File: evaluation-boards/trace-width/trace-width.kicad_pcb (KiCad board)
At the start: 4 copper layers, 80 x 90 mm, 12 parts, among them J1 CONN_COAXIAL, J10 CONN_COAXIAL, J11 CONN_COAXIAL, J12 CONN_COAXIAL, J2 CONN_COAXIAL, J3 CONN_COAXIAL, J4 CONN_COAXIAL, J5 CONN_COAXIAL, J6 CONN_COAXIAL, J7 CONN_COAXIAL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

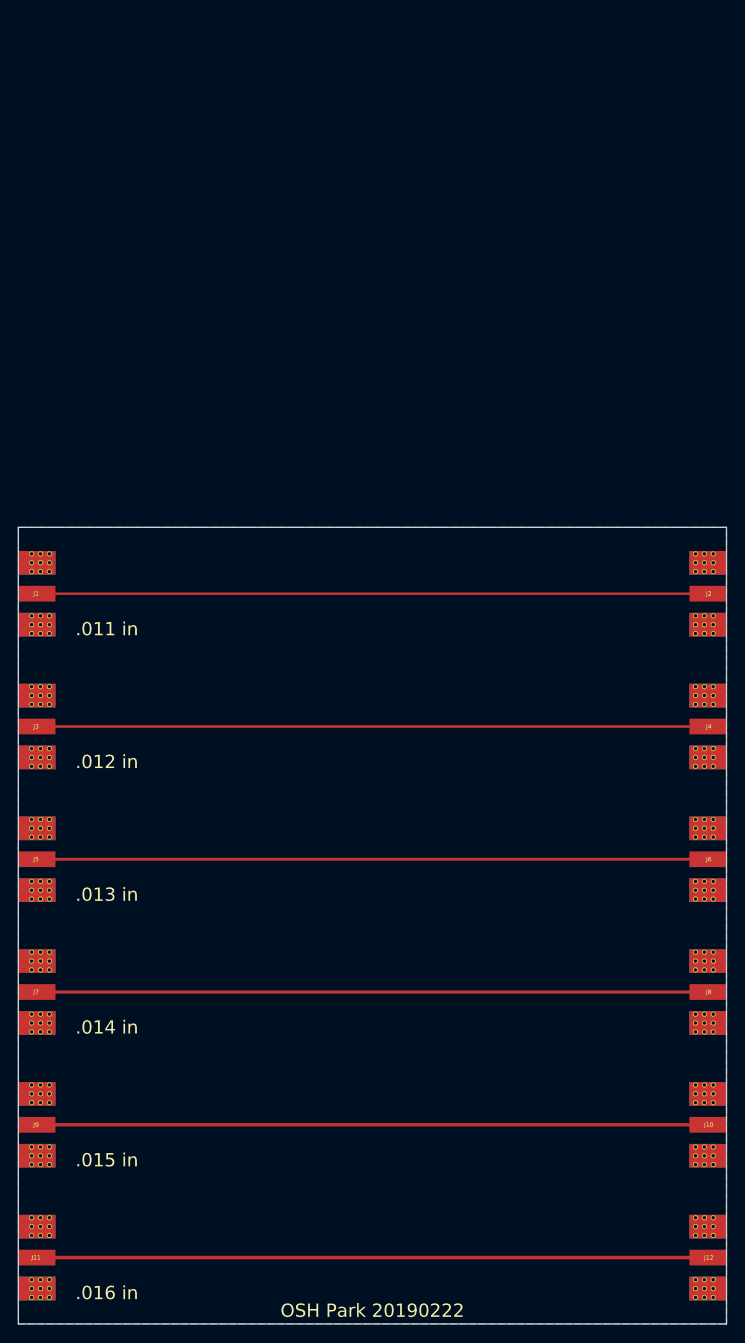
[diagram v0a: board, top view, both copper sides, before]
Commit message: update trace width test board
- widen traces
- use metric widths
- revert to CONSMA003.062 footprint
- add ground plane cutouts under SMA footprint

The schematic wasn't updated as it is not very useful.
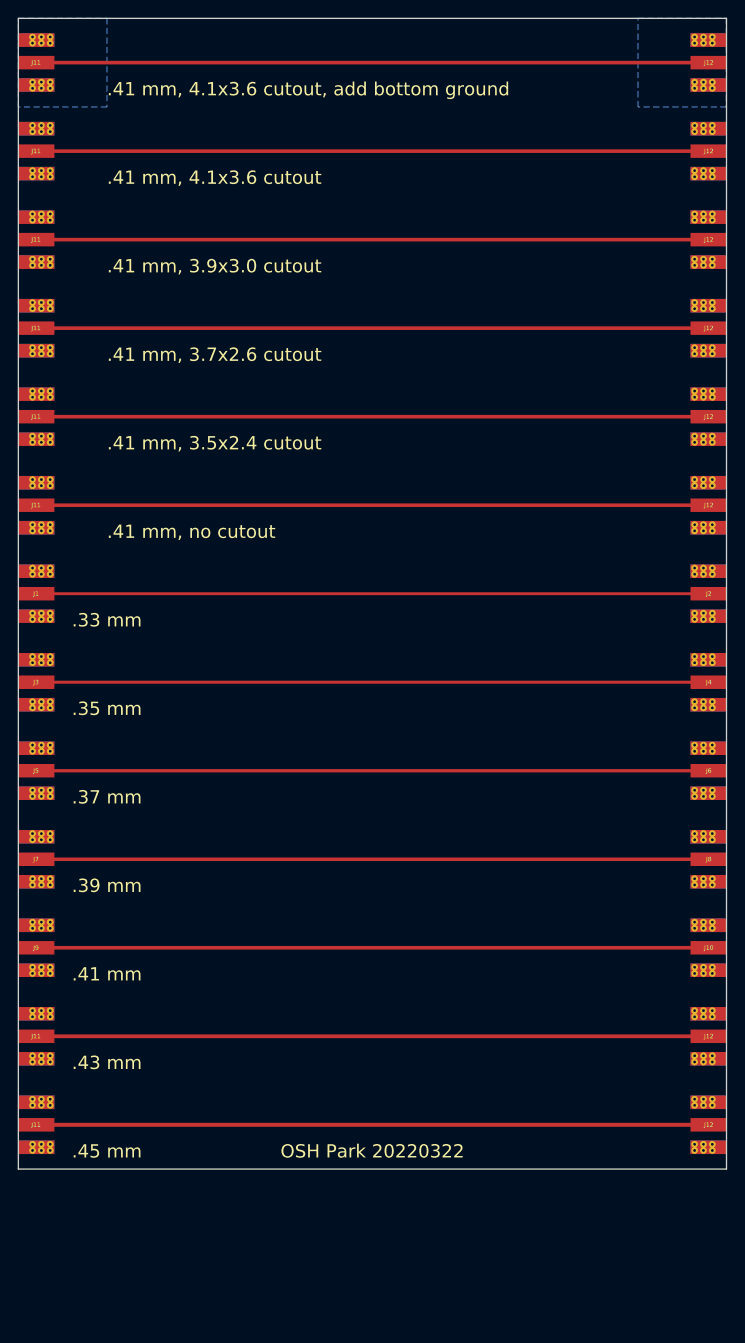
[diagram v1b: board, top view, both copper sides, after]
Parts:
- added J11: CONN_COAXIAL, gsg-modules:SMA-EDGE, F.Cu at (120.0, 20.0)
- added J11: CONN_COAXIAL, gsg-modules:SMA-EDGE, F.Cu at (120.0, 30.0)
- added J11: CONN_COAXIAL, gsg-modules:SMA-EDGE, F.Cu at (120.0, 40.0)
- added J11: CONN_COAXIAL, gsg-modules:SMA-EDGE, F.Cu at (120.0, 50.0)
- added J11: CONN_COAXIAL, gsg-modules:SMA-EDGE, F.Cu at (120.0, 60.0)
- added J11: CONN_COAXIAL, gsg-modules:SMA-EDGE, F.Cu at (120.0, 70.0)
- added J11: CONN_COAXIAL, gsg-modules:SMA-EDGE, F.Cu at (120.0, 140.0)
- added J12: CONN_COAXIAL, gsg-modules:SMA-EDGE, F.Cu at (200.0, 20.0)
- added J12: CONN_COAXIAL, gsg-modules:SMA-EDGE, F.Cu at (200.0, 30.0)
- added J12: CONN_COAXIAL, gsg-modules:SMA-EDGE, F.Cu at (200.0, 40.0)
- added J12: CONN_COAXIAL, gsg-modules:SMA-EDGE, F.Cu at (200.0, 50.0)
- added J12: CONN_COAXIAL, gsg-modules:SMA-EDGE, F.Cu at (200.0, 60.0)
- added J12: CONN_COAXIAL, gsg-modules:SMA-EDGE, F.Cu at (200.0, 70.0)
- added J12: CONN_COAXIAL, gsg-modules:SMA-EDGE, F.Cu at (200.0, 140.0)
- J1, J10, J11, J12, J2, J3, J4, J5, J6, J7, J8, J9: footprint gsg-modules:SMA-73251-2120 -> gsg-modules:SMA-EDGE
- moved J11 25.0 mm to (120.0, 130.0)
- moved J12 25.0 mm to (200.0, 130.0)
- moved J10 20.0 mm to (200.0, 120.0)
- moved J9 20.0 mm to (120.0, 120.0)
- moved J7 15.0 mm to (120.0, 110.0)
- moved J8 15.0 mm to (200.0, 110.0)
- moved J5 10.0 mm to (120.0, 100.0)
- moved J6 10.0 mm to (200.0, 100.0)
- moved J3 5.00 mm to (120.0, 90.0)
- moved J4 5.00 mm to (200.0, 90.0)
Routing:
- net Net-(J11-Pad1): track 75.8 -> 606.5 mm
- removed copper zone on C3, net GND
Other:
- board size 80 x 90 mm -> 80 x 130 mm
- board text added: ".33 mm"
- board text added: ".35 mm"
- board text added: ".37 mm"
- board text added: ".39 mm"
- board text added: ".41 mm"
- board text added: ".41 mm, 3.5x2.4 cutout"
- board text added: ".41 mm, 3.7x2.6 cutout"
- board text added: ".41 mm, 3.9x3.0 cutout"
- board text added: ".41 mm, 4.1x3.6 cutout"
- board text added: ".41 mm, 4.1x3.6 cutout, add bottom ground"
- board text added: ".41 mm, no cutout"
- board text added: ".43 mm"
- board text added: ".45 mm"
- board text added: "OSH Park 20220322"
- board text removed: ".011 in"
- board text removed: ".012 in"
- board text removed: ".013 in"
- board text removed: ".014 in"
- board text removed: ".015 in"
- board text removed: ".016 in"
- board text removed: "OSH Park 20190222"

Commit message: update trace width layout
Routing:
- added copper zone on In1.Cu, net GND
- removed copper zone on C2, net GND
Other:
- net class Default removed
- board text added: ".29 mm"
- board text added: ".30 mm"
- board text added: ".31 mm"
- board text added: ".32 mm"
- board text added: ".33 mm, 3.5x2.4 cutout"
- board text added: ".33 mm, 3.7x2.6 cutout"
- board text added: ".33 mm, 3.9x3.0 cutout"
- board text added: ".33 mm, 4.1x3.6 cutout"
- board text added: ".33 mm, 4.1x3.6 cutout, add bottom ground"
- board text added: ".33 mm, no cutout"
- board text added: ".34 mm"
- board text added: "OSH Park 2022-04-08"
- board text removed: ".37 mm"
- board text removed: ".39 mm"
- board text removed: ".41 mm"
- board text removed: ".41 mm, 3.5x2.4 cutout"
- board text removed: ".41 mm, 3.7x2.6 cutout"
- board text removed: ".41 mm, 3.9x3.0 cutout"
- board text removed: ".41 mm, 4.1x3.6 cutout"
- board text removed: ".41 mm, 4.1x3.6 cutout, add bottom ground"
- board text removed: ".41 mm, no cutout"
- board text removed: ".43 mm"
- board text removed: ".45 mm"
- board text removed: "OSH Park 20220322"
